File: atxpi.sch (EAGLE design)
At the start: 10 parts

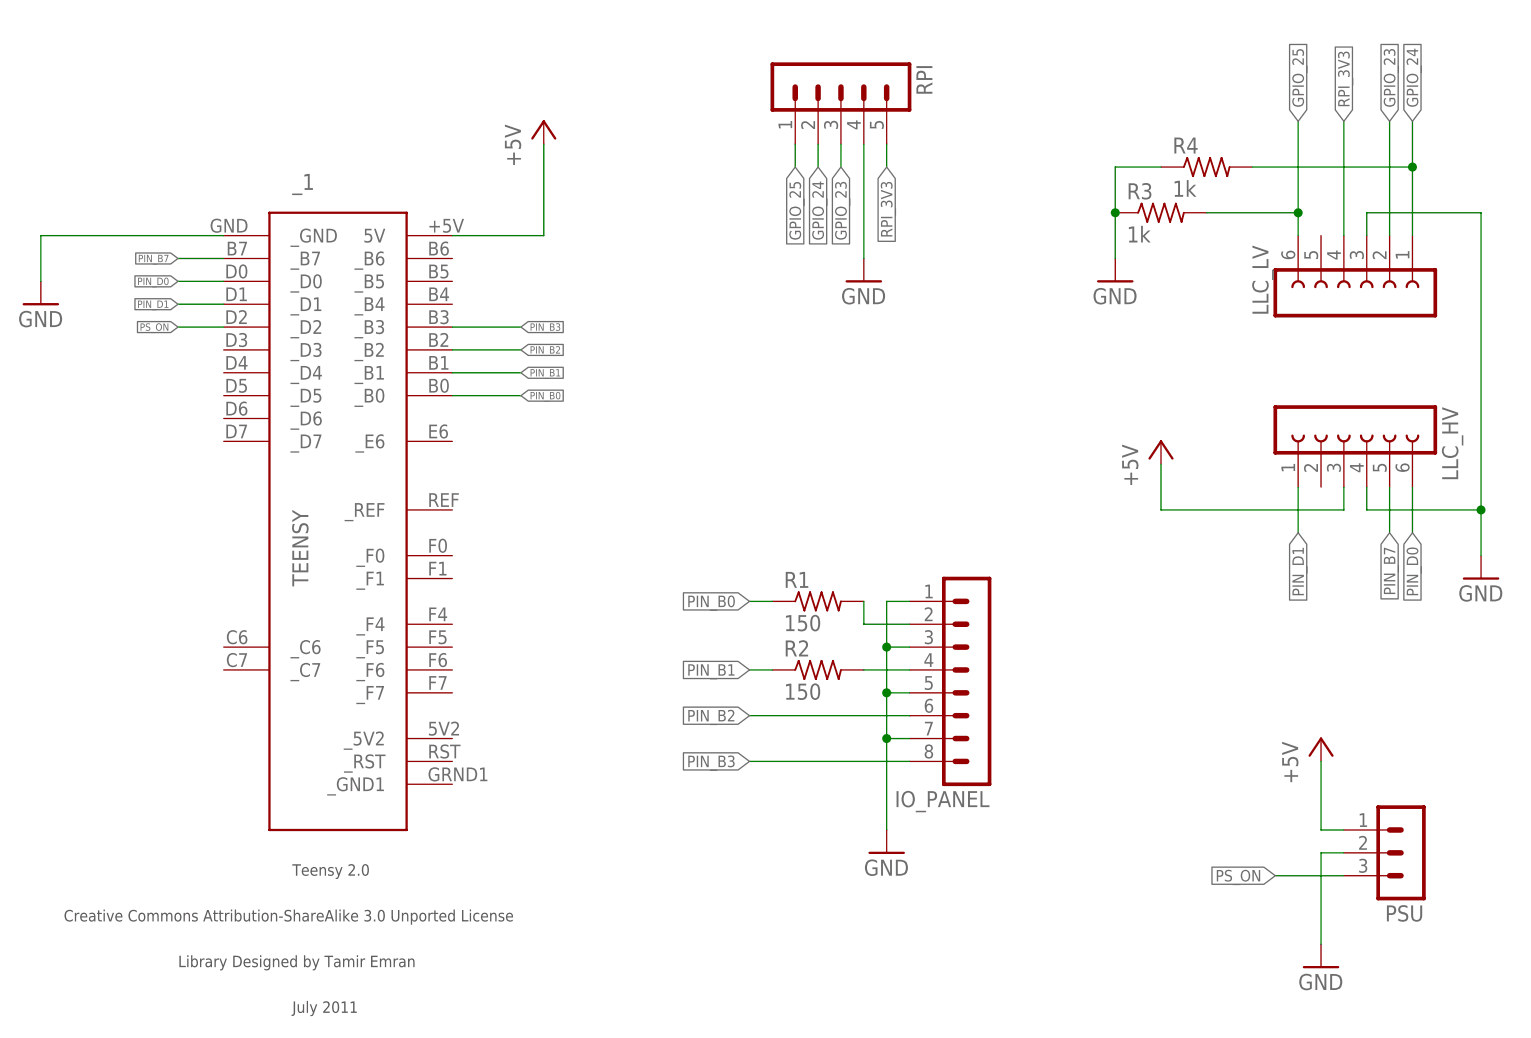
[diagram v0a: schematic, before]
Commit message: update and fix atxpi schematic
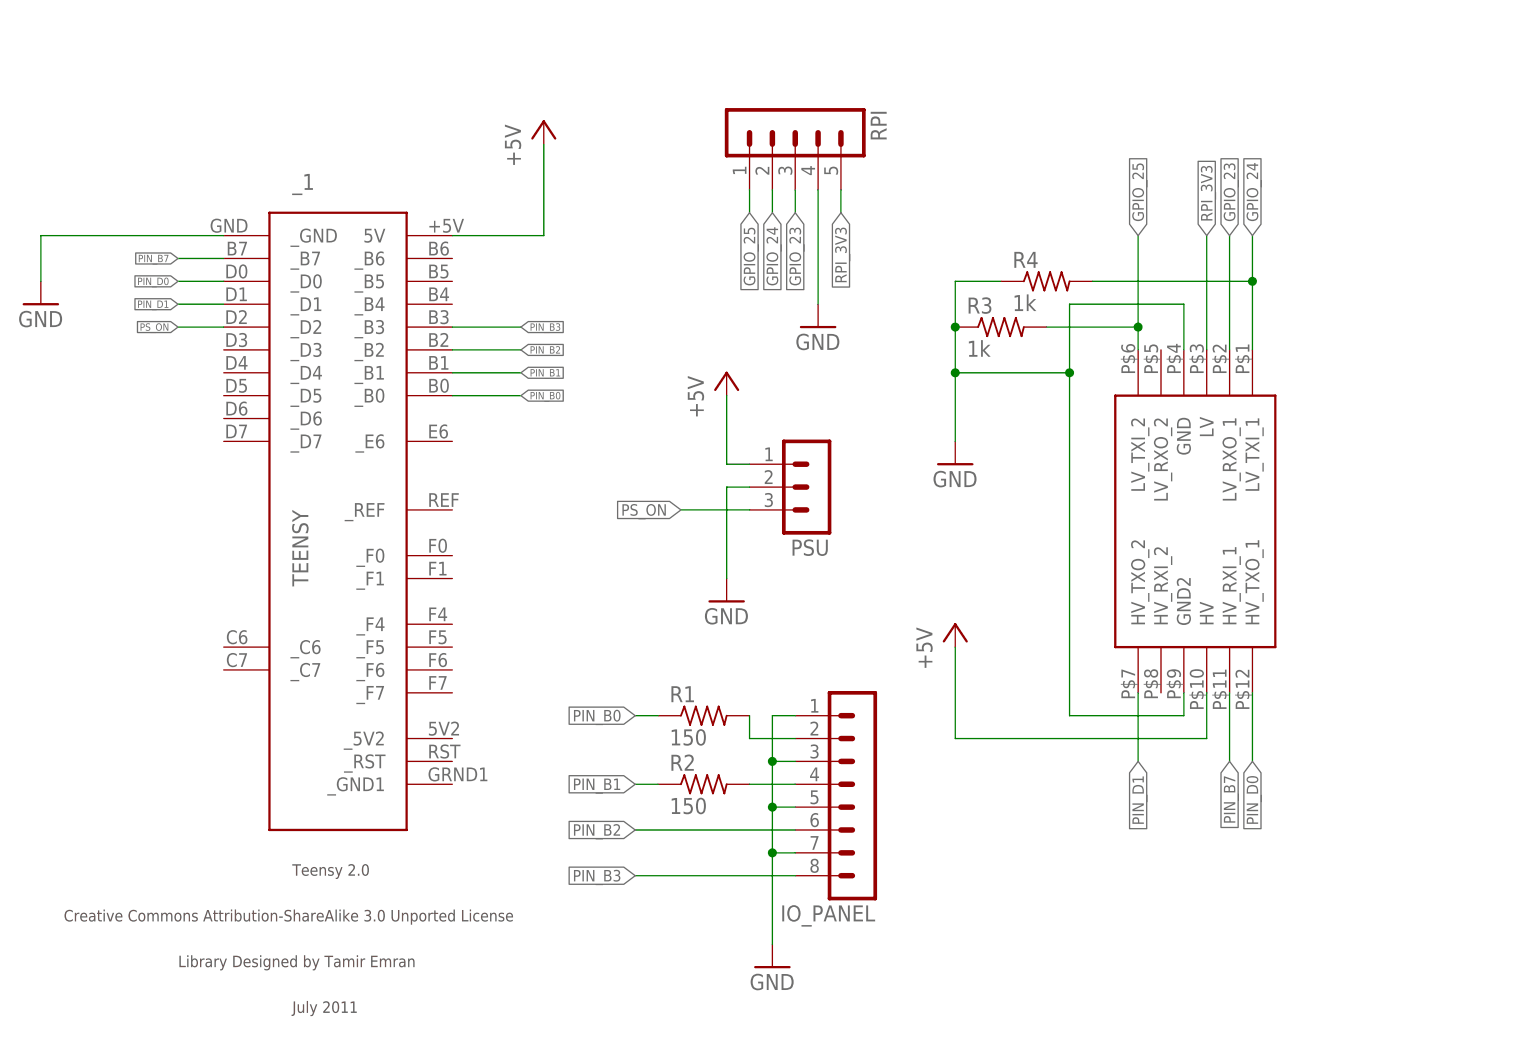
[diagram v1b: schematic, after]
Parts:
- removed LLC_HV, LLC_LV: (no value), con-lsta:FE06-1
- added U$1: LOGIC_LEVEL_CONVERTER, SparkFun-Boards:LOGIC_LEVEL_CONVERTER
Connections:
- net +5V: now also U$1.HV; no longer LLC_HV.3
- net GND: now also U$1.GND, U$1.GND2; no longer LLC_HV.4, LLC_LV.3
- net GPIO_23: now also U$1.LV_RXO_1; no longer LLC_LV.2
- net GPIO_24: now also U$1.LV_TXI_1; no longer LLC_LV.1
- net GPIO_25: now also U$1.LV_TXI_2; no longer LLC_LV.6
- net PIN_B7: now also U$1.HV_RXI_1; no longer LLC_HV.5
- net PIN_D0: now also U$1.HV_TXO_1; no longer LLC_HV.6
- net PIN_D1: now also U$1.HV_TXO_2; no longer LLC_HV.1
- net RPI_3V3: now also U$1.LV; no longer LLC_LV.4
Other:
- moved on the sheet: IO_PANEL, PSU, R1, R2, R3, R4, RPI
